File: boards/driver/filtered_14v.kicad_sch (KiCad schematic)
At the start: 3 parts

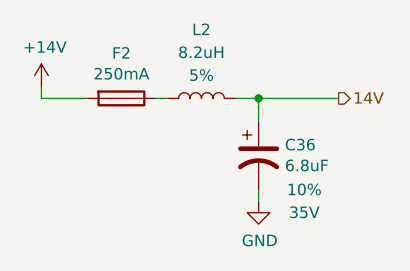
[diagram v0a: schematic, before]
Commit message: Driver: Added a 5V->3.3V LDO to replace the reversed cmod header, added jumpers for the 200R parallel returns, and renamed subcircuit ports to avoid unexpected ground connections.
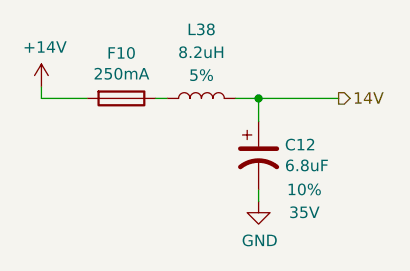
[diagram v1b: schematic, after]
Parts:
- renumbered C36 to C12, F2 to F10, L2 to L38
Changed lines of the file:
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@@
   (symbol (lib_id "Device:Fuse") (at 125.73 96.52 270)
     (in_bom yes) (on_board yes)
-    (property "Reference" "F2" (id 0) (at 125.73 91.5162 90))
+    (property "Reference" "F10" (id 0) (at 125.73 91.5162 90))
     (property "Value" "250mA" (id 1) (at 125.73 93.8276 90))
     (property "Footprint" "" (id 2) (at 125.73 94.742 90)
@@
   (symbol (lib_id "Device:L") (at 134.62 96.52 90)
     (in_bom yes) (on_board yes)
-    (property "Reference" "L2" (id 0) (at 134.62 88.9 90))
+    (property "Reference" "L38" (id 0) (at 134.62 88.9 90))
     (property "Value" "8.2uH" (id 1) (at 134.62 91.44 90))
     (property "Footprint" "Inductor_SMD:L_1812_4532Metric" (id 2) (at 134.62 96.52 0)
@@
   (symbol (lib_id "lachesis:+14V") (at 116.84 95.25 0)
     (in_bom yes) (on_board yes)
-    (property "Reference" "#PWR057" (id 0) (at 116.84 99.06 0)
+    (property "Reference" "#PWR047" (id 0) (at 116.84 99.06 0)
       (effects (font (size 1.27 1.27)) hide)
     )
@@
   (symbol (lib_id "power:GND") (at 140.97 107.95 0)
     (in_bom yes) (on_board yes)
-    (property "Reference" "#PWR058" (id 0) (at 140.97 114.3 0)
+    (property "Reference" "#PWR048" (id 0) (at 140.97 114.3 0)
       (effects (font (size 1.27 1.27)) hide)
     )
@@
   (symbol (lib_id "Device:C_Polarized_US") (at 140.97 102.87 0)
     (in_bom yes) (on_board yes)
-    (property "Reference" "C36" (id 0) (at 143.891 101.7016 0)
+    (property "Reference" "C12" (id 0) (at 143.891 101.7016 0)
       (effects (font (size 1.27 1.27)) (justify left))
     )

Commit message: Driver: incorporated most changes from the test board, and began layout
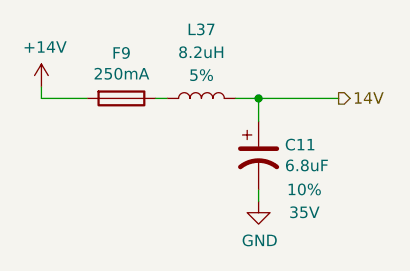
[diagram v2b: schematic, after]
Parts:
- F9: renamed from F10; footprint (none) -> Fuse:Fuse_0603_1608Metric
- L37: renamed from L38; footprint Inductor_SMD:L_1812_4532Metric -> lachesis:API_Delevan_1812R
- renumbered C12 to C11
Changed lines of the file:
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@@
     (effects (font (size 1.27 1.27)) (justify left))
   )
-  (symbol (lib_id "Device:Fuse") (at 125.73 96.52 270)
+  (symbol (lib_id "Device:Fuse") (at 125.73 96.52 270) (unit 1)
     (in_bom yes) (on_board yes)
-    (property "Reference" "F10" (id 0) (at 125.73 91.5162 90))
+    (property "Reference" "F9" (id 0) (at 125.73 91.5162 90))
     (property "Value" "250mA" (id 1) (at 125.73 93.8276 90))
-    (property "Footprint" "" (id 2) (at 125.73 94.742 90)
+    (property "Footprint" "Fuse:Fuse_0603_1608Metric" (id 2) (at 125.73 94.742 90)
       (effects (font (size 1.27 1.27)) hide)
     )
@@
     (pin "2")
   )
-  (symbol (lib_id "Device:L") (at 134.62 96.52 90)
+  (symbol (lib_id "Device:L") (at 134.62 96.52 90) (unit 1)
     (in_bom yes) (on_board yes)
-    (property "Reference" "L38" (id 0) (at 134.62 88.9 90))
+    (property "Reference" "L37" (id 0) (at 134.62 88.9 90))
     (property "Value" "8.2uH" (id 1) (at 134.62 91.44 90))
-    (property "Footprint" "Inductor_SMD:L_1812_4532Metric" (id 2) (at 134.62 96.52 0)
+    (property "Footprint" "lachesis:API_Delevan_1812R" (id 2) (at 134.62 96.52 0)
       (effects (font (size 1.27 1.27)) hide)
     )
@@
     (pin "2")
   )
-  (symbol (lib_id "lachesis:+14V") (at 116.84 95.25 0)
+  (symbol (lib_id "lachesis:+14V") (at 116.84 95.25 0) (unit 1)
     (in_bom yes) (on_board yes)
-    (property "Reference" "#PWR047" (id 0) (at 116.84 99.06 0)
+    (property "Reference" "#PWR045" (id 0) (at 116.84 99.06 0)
       (effects (font (size 1.27 1.27)) hide)
     )
@@
     (pin "1")
   )
-  (symbol (lib_id "power:GND") (at 140.97 107.95 0)
+  (symbol (lib_id "power:GND") (at 140.97 107.95 0) (unit 1)
     (in_bom yes) (on_board yes)
-    (property "Reference" "#PWR048" (id 0) (at 140.97 114.3 0)
+    (property "Reference" "#PWR046" (id 0) (at 140.97 114.3 0)
       (effects (font (size 1.27 1.27)) hide)
     )
@@
     (pin "1")
   )
-  (symbol (lib_id "Device:C_Polarized_US") (at 140.97 102.87 0)
+  (symbol (lib_id "Device:C_Polarized_US") (at 140.97 102.87 0) (unit 1)
     (in_bom yes) (on_board yes)
-    (property "Reference" "C12" (id 0) (at 143.891 101.7016 0)
+    (property "Reference" "C11" (id 0) (at 143.891 101.7016 0)
       (effects (font (size 1.27 1.27)) (justify left))
     )
